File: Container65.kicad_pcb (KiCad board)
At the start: 2 copper layers, 77 x 95.2 mm, 1 part

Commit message: Design
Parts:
- removed USB1: HRO-TYPE-C-31-M-12, Type-C:HRO-TYPE-C-31-M-12-Assembly
- added C1: 1uF, Keebio-Parts:C_0402, B.Cu at (100.4, -25.5)
- added C10: 100nF, Keebio-Parts:C_0402, B.Cu at (61.2, -64.9)
- added C11: 100nF, Keebio-Parts:C_0402, B.Cu at (112.3, -17.1)
- added C12: 100nF, Keebio-Parts:C_0402, B.Cu at (141.3, 17.2)
- added C13: 100nF, Keebio-Parts:C_0402, B.Cu at (112.3, -10.9)
- added C14: 100nF, Keebio-Parts:C_0402, B.Cu at (42.1, -83.1)
- added C15: 100nF, Keebio-Parts:C_0402, B.Cu at (139.7, 13.2)
- added C16: 100nF, Keebio-Parts:C_0402, B.Cu at (121.6, -3.68)
- added C17: 100nF, Keebio-Parts:C_0402, B.Cu at (119.5, -6.31)
- added C18: 0.1 uF, Keebio-Parts:C_0402, B.Cu at (42.1, -85.1)
- added C2: 1uF, Keebio-Parts:C_0402, B.Cu at (42.1, -81.0)
- added C3: 0.1 uF, Keebio-Parts:C_0402, B.Cu at (109.1, -16.7)
- added C4: 1uF, Keebio-Parts:C_0402, B.Cu at (112.3, -13.0)
- added C5: 1uF, Keebio-Parts:C_0402, B.Cu at (97.3, -27.5)
- added C6: 30pF, Keebio-Parts:C_0402, B.Cu at (132.5, 8.08)
- added C7: 30pF, Keebio-Parts:C_0402, B.Cu at (132.5, 6.02)
- added C8: 100nF, Keebio-Parts:C_0402, B.Cu at (100.4, -27.5)
- added C9: 100nF, Keebio-Parts:C_0402, B.Cu at (112.3, -15.0)
- added D1: 1N4148W, Keebio-Parts:D_SOD123, B.Cu at (60.3, 54.0)
- added D10: 1N4148W, Keebio-Parts:D_SOD123, B.Cu at (64.3, 92.1)
- added D11: 1N4148W, Keebio-Parts:D_SOD123, B.Cu at (91.3, 92.1)
- added D12: 1N4148W, Keebio-Parts:D_SOD123, B.Cu at (95.2, 92.1)
- added D13: 1N4148W, Keebio-Parts:D_SOD123, B.Cu at (60.3, 111.1)
- added D14: 1N4148W, Keebio-Parts:D_SOD123, B.Cu at (64.3, 111.1)
- added D15: 1N4148W, Keebio-Parts:D_SOD123, B.Cu at (91.3, 111.1)
- added D16: 1N4148W, Keebio-Parts:D_SOD123, B.Cu at (95.2, 111.1)
- added D17: 1N4148W, Keebio-Parts:D_SOD123, B.Cu at (43.7, 129.4)
- added D18: 1N4148W, Keebio-Parts:D_SOD123, B.Cu at (75.4, 129.4)
- added D19: 1N4148W, Keebio-Parts:D_SOD123, B.Cu at (80.2, 129.4)
- added D2: 1N4148W, Keebio-Parts:D_SOD123, B.Cu at (64.3, 54.0)
- added D20: 1N4148W, Keebio-Parts:D_SOD123, B.Cu at (111.9, 129.4)
- added D21: Schottky 5819W, Keebio-Parts:D_SOD123, B.Cu at (116.3, 19.8)
- added D22: Power LED (Blue), Keebio-Parts:R_0805, B.Cu at (95.0, -31.7)
- added D3: 1N4148W, Keebio-Parts:D_SOD123, B.Cu at (91.3, 54.0)
- added D4: 1N4148W, Keebio-Parts:D_SOD123, B.Cu at (95.2, 54.0)
- added D5: 1N4148W, Keebio-Parts:D_SOD123, B.Cu at (60.3, 73.0)
- added D6: 1N4148W, Keebio-Parts:D_SOD123, B.Cu at (64.3, 73.0)
- added D7: 1N4148W, Keebio-Parts:D_SOD123, B.Cu at (91.3, 73.0)
- added D8: 1N4148W, Keebio-Parts:D_SOD123, B.Cu at (95.2, 73.0)
- added D9: 1N4148W, Keebio-Parts:D_SOD123, B.Cu at (60.3, 92.1)
- added F1: TLC_PSMD050, Keebio-Parts:Fuse_0805, B.Cu at (99.9, -30.0)
- added FB1: 100@100MHz, Inductor_SMD:L_0805_2012Metric, B.Cu at (94.8, -34.6)
- added J1: Conn_01x03, Connector_PinHeader_2.54mm:PinHeader_1x03_P2.54mm_Vertical, B.Cu at (138.9, -2.38)
- added J2: Conn_01x06, Connector_PinHeader_1.27mm:PinHeader_1x06_P1.27mm_Vertical, B.Cu at (134.5, -3.03)
- added MX-E-1: MX-2U, Switch_Keyboard_Hotswap_Kailh:SW_Hotswap_Kailh_MX_1.00u_Extras, F.Cu at (106.4, 77.0)
- added MX-E-2: MX-2U, Switch_Keyboard_Hotswap_Kailh:SW_Hotswap_Kailh_MX_1.00u_Extras, F.Cu at (106.4, 115.1)
- added MX-E-3: MX-2U, Switch_Keyboard_Hotswap_Kailh:SW_Hotswap_Kailh_MX_1.00u_Extras, F.Cu at (58.7, 124.6)
- added MX-E-4: MX-2U, Switch_Keyboard_Hotswap_Kailh:SW_Hotswap_Kailh_MX_1.00u_Extras, F.Cu at (96.8, 124.6)
- added MX-E-5: MX-2U, Switch_Keyboard_Hotswap_Kailh:SW_Hotswap_Kailh_MX_1.00u_Extras, F.Cu at (49.2, 77.0)
- added MX-E-6: MX-2U, Switch_Keyboard_Hotswap_Kailh:SW_Hotswap_Kailh_MX_1.00u_Extras, F.Cu at (49.2, 115.1)
- added MX1: MX-1U, Switch_Keyboard_Hotswap_Kailh:SW_Hotswap_Kailh_MX_1.00u_Modified, F.Cu at (49.2, 48.4)
- added MX10: MX-1U, Switch_Keyboard_Hotswap_Kailh:SW_Hotswap_Kailh_MX_1.00u_Modified, F.Cu at (68.3, 86.5)
- added MX11: MX-1U, Switch_Keyboard_Hotswap_Kailh:SW_Hotswap_Kailh_MX_1.00u_Modified, F.Cu at (87.3, 86.5)
- added MX12: MX-1U, Switch_Keyboard_Hotswap_Kailh:SW_Hotswap_Kailh_MX_1.00u_Modified, F.Cu at (106.4, 86.5)
- added MX13: MX-1U, Switch_Keyboard_Hotswap_Kailh:SW_Hotswap_Kailh_MX_1.00u_Modified, F.Cu at (49.2, 105.6)
- added MX14: MX-1U, Switch_Keyboard_Hotswap_Kailh:SW_Hotswap_Kailh_MX_1.00u_Modified, F.Cu at (68.3, 105.6)
- added MX15: MX-1U, Switch_Keyboard_Hotswap_Kailh:SW_Hotswap_Kailh_MX_1.00u_Modified, F.Cu at (87.3, 105.6)
- added MX16: MX-1U, Switch_Keyboard_Hotswap_Kailh:SW_Hotswap_Kailh_MX_1.00u_Modified, F.Cu at (106.4, 105.6)
- added MX17: MX-1U, Switch_Keyboard_Hotswap_Kailh:SW_Hotswap_Kailh_MX_1.00u_Modified, F.Cu at (49.2, 124.6)
- added MX18: MX-1U, Switch_Keyboard_Hotswap_Kailh:SW_Hotswap_Kailh_MX_1.00u_Modified, F.Cu at (68.3, 124.6)
- added MX19: MX-1U, Switch_Keyboard_Hotswap_Kailh:SW_Hotswap_Kailh_MX_1.00u_Modified, F.Cu at (87.3, 124.6)
- added MX2: MX-1U, Switch_Keyboard_Hotswap_Kailh:SW_Hotswap_Kailh_MX_1.00u_Modified, F.Cu at (68.3, 48.4)
- added MX20: MX-1U, Switch_Keyboard_Hotswap_Kailh:SW_Hotswap_Kailh_MX_1.00u_Modified, F.Cu at (106.4, 124.6)
- added MX3: MX-1U, Switch_Keyboard_Hotswap_Kailh:SW_Hotswap_Kailh_MX_1.00u_Modified, F.Cu at (87.3, 48.4)
- added MX4: MX-1U, Switch_Keyboard_Hotswap_Kailh:SW_Hotswap_Kailh_MX_1.00u_Modified, F.Cu at (106.4, 48.4)
- added MX5: MX-1U, Switch_Keyboard_Hotswap_Kailh:SW_Hotswap_Kailh_MX_1.00u_Modified, F.Cu at (49.2, 67.5)
- added MX6: MX-1U, Switch_Keyboard_Hotswap_Kailh:SW_Hotswap_Kailh_MX_1.00u_Modified, F.Cu at (68.3, 67.5)
- added MX7: MX-1U, Switch_Keyboard_Hotswap_Kailh:SW_Hotswap_Kailh_MX_1.00u_Modified, F.Cu at (87.3, 67.5)
- added MX8: MX-1U, Switch_Keyboard_Hotswap_Kailh:SW_Hotswap_Kailh_MX_1.00u_Modified, F.Cu at (106.4, 67.5)
- added MX9: MX-1U, Switch_Keyboard_Hotswap_Kailh:SW_Hotswap_Kailh_MX_1.00u_Modified, F.Cu at (49.2, 86.5)
- added POGO1: Conn_01x06_Male, extras:1x04_3.00mm_Magnetic Pogo_Male, F.Cu at (43.4, 54.8)
- added POGO2: Conn_01x06_Female, extras:1x04_3.00mm_Magnetic Pogo_Female_2, F.Cu at (112.2, 54.8)
- added R1: 27 ohm, Keebio-Parts:R_0402, B.Cu at (129.6, 5.67)
- added R2: 27 ohm, Keebio-Parts:R_0402, B.Cu at (121.8, -1.56)
- added R3: 1k ohm, Keebio-Parts:R_0402, B.Cu at (102.2, -21.2)
- added R4: 10k ohm, Keebio-Parts:R_0402, B.Cu at (39.2, -85.1)
- added R5: 1k ohm, Keebio-Parts:R_0402, B.Cu at (109.4, -14.6)
- added R6: 5.1k, Keebio-Parts:R_0402, B.Cu at (58.3, -64.9)
- added R7: 5.1k, Keebio-Parts:R_0402, B.Cu at (102.2, -23.4)
- added R8: 10k ohm, Keebio-Parts:R_0402, B.Cu at (61.4, -62.8)
- added R9: 1k5 ohm, Keebio-Parts:R_0402, B.Cu at (136.8, 13.3)
- added U1: RP2040, extras:rp2040, B.Cu at (127.8, -0.06)
- added U2: TYPE-C-31-M-12, extras:simple-usb-c, B.Cu at (58.7, 35.7)
- added U3: XC6206PxxxMR, Package_TO_SOT_SMD:SOT-23, B.Cu at (99.5, -33.7)
- added U4: W25Q128JVS, Package_SO:SOIC-8_5.23x5.23mm_P1.27mm, B.Cu at (115.9, -21.5)
- added U5: USB Boot, extras:tactile-switch, B.Cu at (153.2, 75.4)
- added U6: Reset, extras:tactile-switch, B.Cu at (111.1, 3.17)
- added U7: LEFT, Keebio-Parts:TRRS-PJ-320A, B.Cu at (39.3, 92.9)
- added U8: RIGHT, Keebio-Parts:TRRS-PJ-320A, B.Cu at (116.2, 92.9)
- added Y1: 12MHz - 20pF, Crystal:Crystal_SMD_3225-4Pin_3.2x2.5mm, B.Cu at (88.7, -36.3)
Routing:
- net (no net): track 23.2 -> 0.00 mm
- net Net-(D1-Pad2): track 0.00 -> 1.47 mm
- removed copper zone on B.Cu, net (none)
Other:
- board size 77 x 95.2 mm -> 81 x 99.2 mm

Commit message: Copy from backup
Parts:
- U7, U8: footprint Keebio-Parts:TRRS-PJ-320A -> Keebio-Parts:TRRS-PJ-320D
- moved U8 4.83 mm to (121.0, 92.1)
- moved U7 4.83 mm to (34.6, 92.1)
- moved POGO1 1.89 mm to (41.5, 54.8)
- moved POGO2 1.88 mm to (114.1, 54.9)
- moved D20 1.59 mm to (110.3, 129.4)
- moved D17 1.59 mm to (45.2, 129.4)
- moved U2 0.79 mm to (58.7, 36.5)
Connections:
- U7 pad 1: unconnected-(U7-Pad1) -> SCL
- U7 pad 2: unconnected-(U7-Pad2) -> VCC
- U7 pad 3: unconnected-(U7-Pad3) -> GND
- U7 pad 4: unconnected-(U7-Pad4) -> SDA
- U8 pad 1: unconnected-(U8-Pad1) -> SCL
- U8 pad 2: unconnected-(U8-Pad2) -> VCC
- U8 pad 3: unconnected-(U8-Pad3) -> GND
- U8 pad 4: unconnected-(U8-Pad4) -> SDA
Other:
- board size 81 x 99.2 mm -> 84.1 x 99.2 mm

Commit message: Board edits
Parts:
- moved U7 0.79 mm to (34.6, 92.9)
- moved U8 0.79 mm to (121.0, 92.9)
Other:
- board size 84.1 x 99.2 mm -> 84.1 x 100 mm
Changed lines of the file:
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@@
   )
   (footprint "Keebio-Parts:TRRS-PJ-320D" locked (layer "B.Cu")
-    (at 121 92.075 90)
+    (at 121 92.86875 90)
     (property "Sheetfile" "Container65.kicad_sch")
     (property "Sheetname" "")
@@
   )
   (footprint "Keebio-Parts:TRRS-PJ-320D" locked (layer "B.Cu")
-    (at 34.575 92.075 -90)
+    (at 34.575 92.86875 -90)
     (property "Sheetfile" "Container65.kicad_sch")
     (property "Sheetname" "")
@@
   (gr_line (start 106.3625 48.41875) (end 123.03125 48.41875) (layer "Cmts.User") (width 0.1))
   (gr_line (start 123.03125 66.675) (end 123.03125 97.63125) (layer "Cmts.User") (width 0.1))
-  (gr_line (start 115.09375 100.80625) (end 115.09375 130.96875) (layer "Edge.Cuts") (width 0.15))
-  (gr_line (start 112.7125 133.35) (end 42.8625 133.35) (layer "Edge.Cuts") (width 0.15))
+  (gr_line (start 42.06875 38.89375) (end 53.18125 38.89375) (layer "Edge.Cuts") (width 0.15))
+  (gr_line (start 115.8875 100.80625) (end 115.8875 131.7625) (layer "Edge.Cuts") (width 0.15))
+  (gr_arc (start 115.8875 69.05625) (mid 116.352493 67.933743) (end 117.475 67.46875) (layer "Edge.Cuts") (width 0.15))
+  (gr_line (start 113.50625 134.14375) (end 42.06875 134.14375) (layer "Edge.Cuts") (width 0.15))
+  (gr_arc (start 38.1 99.21875) (mid 39.222507 99.683743) (end 39.6875 100.80625) (layer "Edge.Cuts") (width 0.15))
+  (gr_line (start 38.1 86.51875) (end 37.30625 86.51875) (layer "Edge.Cuts") (width 0.15))
+  (gr_arc (start 41.275 39.6875) (mid 41.042503 40.248753) (end 40.48125 40.48125) (layer "Edge.Cuts") (width 0.15))
   (gr_arc locked (start 53.975 34.925) (mid 54.207528 34.363778) (end 54.76875 34.13125) (layer "Edge.Cuts") (width 0.15))
-  (gr_arc (start 115.09375 100.80625) (mid 115.791231 99.122481) (end 117.475 98.425) (layer "Edge.Cuts") (width 0.15))
-  (gr_line (start 53.975 39.6875) (end 53.975 34.925) (layer "Edge.Cuts") (width 0.15))
+  (gr_line (start 118.26875 67.46875) (end 117.475 67.46875) (layer "Edge.Cuts") (width 0.15))
+  (gr_line (start 118.26875 99.21875) (end 117.475 99.21875) (layer "Edge.Cuts") (width 0.15))
+  (gr_line (start 53.975 38.1) (end 53.975 34.925) (layer "Edge.Cuts") (width 0.15))
+  (gr_arc (start 115.8875 100.80625) (mid 116.352493 99.683743) (end 117.475 99.21875) (layer "Edge.Cuts") (width 0.15))
+  (gr_arc (start 117.475 86.51875) (mid 116.352495 86.053755) (end 115.8875 84.93125) (layer "Edge.Cuts") (width 0.15))
+  (gr_arc (start 113.50625 38.89375) (mid 114.067556 39.126194) (end 114.3 39.6875) (layer "Edge.Cuts") (width 0.15))
+  (gr_arc (start 119.85625 97.63125) (mid 119.391256 98.753756) (end 118.26875 99.21875) (layer "Edge.Cuts") (width 0.15))
   (gr_arc (start 117.475 40.48125) (mid 119.158827 41.178673) (end 119.85625 42.8625) (layer "Edge.Cuts") (width 0.15))
-  (gr_arc (start 42.8625 133.35) (mid 41.178702 132.652548) (end 40.48125 130.96875) (layer "Edge.Cuts") (width 0.15))
+  (gr_arc (start 42.06875 134.14375) (mid 40.384934 133.446301) (end 39.6875 131.7625) (layer "Edge.Cuts") (width 0.15))
+  (gr_arc (start 118.26875 86.51875) (mid 119.391257 86.983743) (end 119.85625 88.10625) (layer "Edge.Cuts") (width 0.15))
   (gr_arc (start 35.71875 42.8625) (mid 36.416202 41.178702) (end 38.1 40.48125) (layer "Edge.Cuts") (width 0.15))
-  (gr_arc (start 115.09375 130.96875) (mid 114.396298 132.652548) (end 112.7125 133.35) (layer "Edge.Cuts") (width 0.15))
-  (gr_line (start 63.5 34.925) (end 63.5 39.6875) (layer "Edge.Cuts") (width 0.15))
-  (gr_line (start 35.71875 96.04375) (end 35.71875 42.8625) (layer "Edge.Cuts") (width 0.15))
-  (gr_arc (start 119.85625 96.04375) (mid 119.158769 97.727519) (end 117.475 98.425) (layer "Edge.Cuts") (width 0.15))
-  (gr_arc locked (start 53.975 39.6875) (mid 53.742531 40.248781) (end 53.18125 40.48125) (layer "Edge.Cuts") (width 0.15))
-  (gr_line (start 40.48125 130.96875) (end 40.48125 100.80625) (layer "Edge.Cuts") (width 0.15))
-  (gr_arc locked (start 64.29375 40.48125) (mid 63.732499 40.248751) (end 63.5 39.6875) (layer "Edge.Cuts") (width 0.15))
+  (gr_arc (start 115.8875 131.7625) (mid 115.19003 133.446266) (end 113.50625 134.14375) (layer "Edge.Cuts") (width 0.15))
+  (gr_arc (start 38.1 67.46875) (mid 39.222507 67.933743) (end 39.6875 69.05625) (layer "Edge.Cuts") (width 0.15))
+  (gr_line (start 63.5 34.925) (end 63.5 38.1) (layer "Edge.Cuts") (width 0.15))
+  (gr_line (start 35.71875 65.88125) (end 35.71875 42.8625) (layer "Edge.Cuts") (width 0.15))
+  (gr_arc (start 35.71875 88.10625) (mid 36.183743 86.983743) (end 37.30625 86.51875) (layer "Edge.Cuts") (width 0.15))
+  (gr_arc (start 37.30625 99.21875) (mid 36.183744 98.753756) (end 35.71875 97.63125) (layer "Edge.Cuts") (width 0.15))
+  (gr_line (start 39.6875 84.93125) (end 39.6875 69.05625) (layer "Edge.Cuts") (width 0.15))
+  (gr_arc (start 119.85625 65.88125) (mid 119.391256 67.003756) (end 118.26875 67.46875) (layer "Edge.Cuts") (width 0.15))
+  (gr_line (start 115.09375 40.48125) (end 117.475 40.48125) (layer "Edge.Cuts") (width 0.15))
+  (gr_line (start 119.85625 42.8625) (end 119.85625 65.88125) (layer "Edge.Cuts") (width 0.15))
+  (gr_arc (start 41.275 39.6875) (mid 41.507497 39.126247) (end 42.06875 38.89375) (layer "Edge.Cuts") (width 0.15))
+  (gr_line (start 35.71875 97.63125) (end 35.71875 88.10625) (layer "Edge.Cuts") (width 0.15))
+  (gr_line (start 38.1 99.21875) (end 37.30625 99.21875) (layer "Edge.Cuts") (width 0.15))
+  (gr_arc locked (start 53.975 38.1) (mid 53.742548 38.661313) (end 53.18125 38.89375) (layer "Edge.Cuts") (width 0.15))
+  (gr_line (start 39.6875 131.7625) (end 39.6875 100.80625) (layer "Edge.Cuts") (width 0.15))
+  (gr_arc locked (start 64.29375 38.89375) (mid 63.732481 38.661254) (end 63.5 38.1) (layer "Edge.Cuts") (width 0.15))
+  (gr_line (start 64.29375 38.89375) (end 113.50625 38.89375) (layer "Edge.Cuts") (width 0.15))
+  (gr_arc (start 39.6875 84.93125) (mid 39.222505 86.053755) (end 38.1 86.51875) (layer "Edge.Cuts") (width 0.15))
+  (gr_line (start 38.1 67.46875) (end 37.30625 67.46875) (layer "Edge.Cuts") (width 0.15))
   (gr_arc locked (start 62.70625 34.13125) (mid 63.267531 34.363719) (end 63.5 34.925) (layer "Edge.Cuts") (width 0.15))
-  (gr_arc (start 38.1 98.425) (mid 39.783769 99.122481) (end 40.48125 100.80625) (layer "Edge.Cuts") (width 0.15))
-  (gr_line (start 64.29375 40.48125) (end 117.475 40.48125) (layer "Edge.Cuts") (width 0.15))
-  (gr_arc (start 38.1 98.425) (mid 36.416231 97.727519) (end 35.71875 96.04375) (layer "Edge.Cuts") (width 0.15))
+  (gr_line (start 115.8875 69.05625) (end 115.8875 84.93125) (layer "Edge.Cuts") (width 0.15))
+  (gr_arc (start 115.09375 40.48125) (mid 114.532444 40.248806) (end 114.3 39.6875) (layer "Edge.Cuts") (width 0.15))
+  (gr_line (start 119.85625 88.10625) (end 119.85625 97.63125) (layer "Edge.Cuts") (width 0.15))
+  (gr_line (start 118.26875 86.51875) (end 117.475 86.51875) (layer "Edge.Cuts") (width 0.15))
+  (gr_arc (start 37.30625 67.46875) (mid 36.183744 67.003756) (end 35.71875 65.88125) (layer "Edge.Cuts") (width 0.15))
   (gr_line locked (start 54.76875 34.13125) (end 62.70625 34.13125) (layer "Edge.Cuts") (width 0.15))
-  (gr_line (start 119.85625 96.04375) (end 119.85625 42.8625) (layer "Edge.Cuts") (width 0.15))
-  (gr_line (start 38.1 40.48125) (end 53.18125 40.48125) (layer "Edge.Cuts") (width 0.15))
+  (gr_line (start 38.1 40.48125) (end 40.48125 40.48125) (layer "Edge.Cuts") (width 0.15))
   (dimension (type aligned) (layer "Edge.Cuts")
     (pts (xy 123.03125 48.41875) (xy 106.3625 48.41875))

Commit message: Added OLED
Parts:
- removed POGO1: Conn_01x06_Male, extras:1x04_3.00mm_Magnetic Pogo_Male
- removed POGO2: Conn_01x06_Female, extras:1x04_3.00mm_Magnetic Pogo_Female_2
- added J3: POGOm1, extras:1x02_2.54_Pogo Male GND, F.Cu at (30.4, 52.9)
- added J4: POGOm2, extras:1x02_2.54_Pogo Male, F.Cu at (31.2, 58.7)
- added J5: POGOf1, extras:1x02_2.54_Pogo Female GND, F.Cu at (87.1, 17.5)
- added J6: POGOf2, extras:1x02_2.54_Pogo Female, F.Cu at (87.1, 23.8)
- moved J1 6.35 mm to (145.3, -2.38)

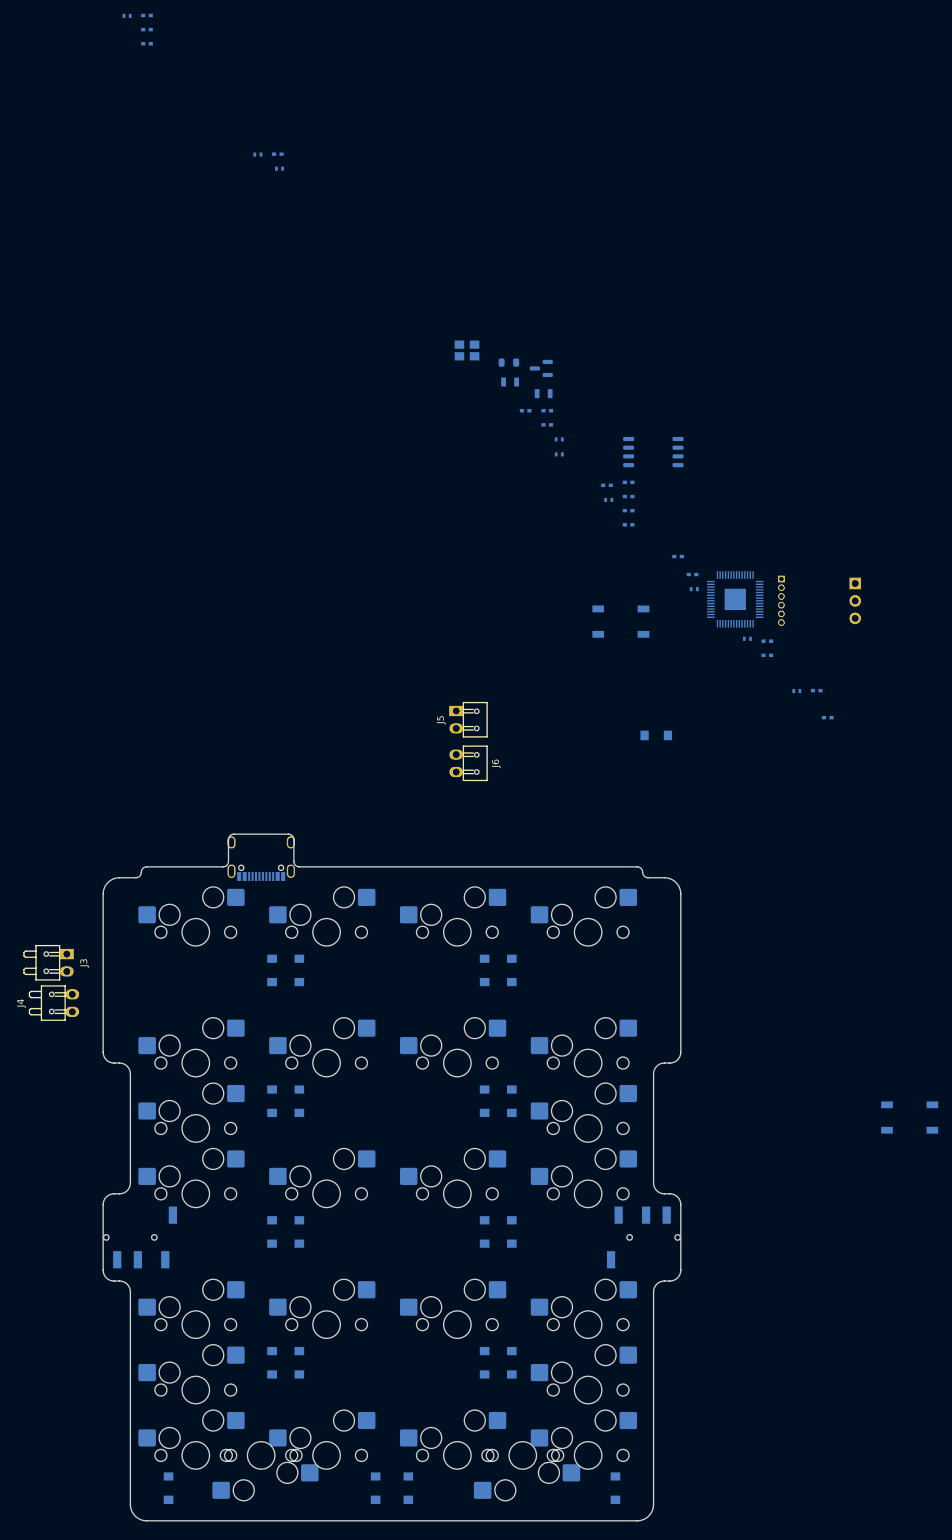
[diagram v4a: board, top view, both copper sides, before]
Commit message: Removed 1u
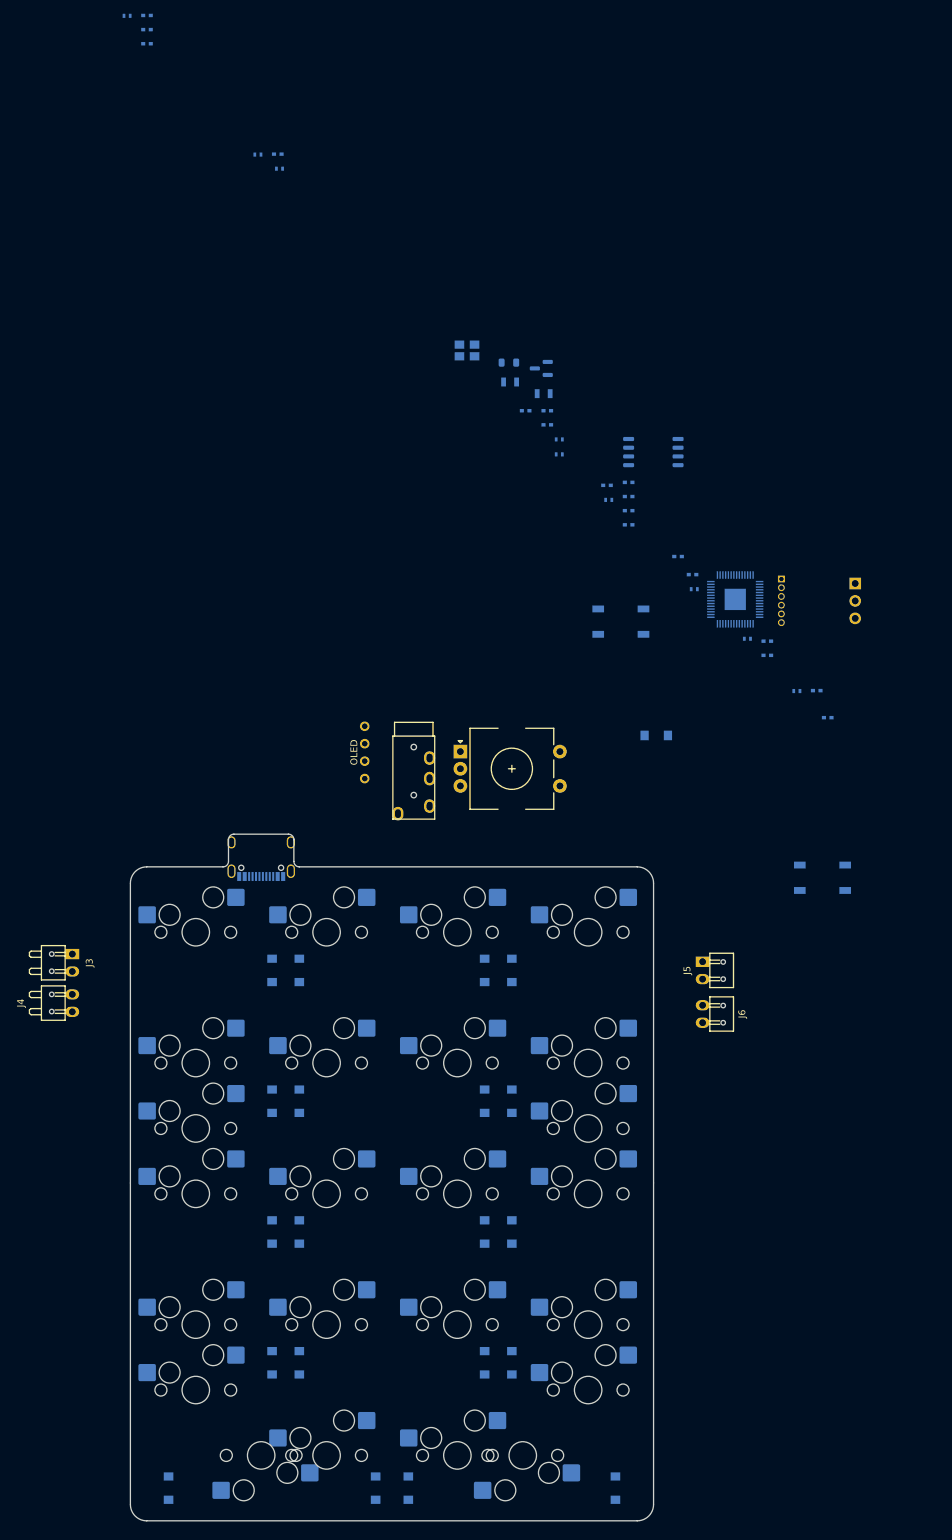
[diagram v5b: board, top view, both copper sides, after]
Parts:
- removed the MX17 at (49.2, 124.6)
- removed the MX20 at (106.4, 124.6)
- removed U8: RIGHT, Keebio-Parts:TRRS-PJ-320D
- added OL1: OLED, kbd:OLED_v2, F.Cu at (73.8, 22.2)
- added SW1: RotaryEncoder_Switch, Keebio-Parts:RotaryEncoder_EC11, F.Cu at (95.2, 24.6)
- U7: value LEFT -> TRRS; footprint Keebio-Parts:TRRS-PJ-320D -> Keebio-Parts:TRRS-PJ-320A; moved to F.Cu
- moved U7 86.5 mm to (81.0, 19.8), turned to 0 degrees
- moved J5 51.2 mm to (123.0, 54.0)
- moved J6 51.2 mm to (123.0, 60.3)
- moved U5 37.2 mm to (140.5, 40.5)
- moved J3 0.79 mm to (31.2, 52.9)
- renumbered MX-E-5 to MX-E-1, MX-E-1 to MX-E-2, MX-E-6 to MX-E-3, MX-E-3 to MX17, MX-E-2 to MX20
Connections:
- J3 pad 2: SDA -> VCC
- J4 pad 1: SCL -> SDA
- J4 pad 2: VCC -> SCL
- J5 pad 2: SDA -> VCC
- J6 pad 1: SCL -> SDA
- J6 pad 2: VCC -> SCL
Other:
- board size 84.1 x 100 mm -> 76.2 x 100 mm
